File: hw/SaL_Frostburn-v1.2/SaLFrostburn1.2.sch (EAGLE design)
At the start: 99 parts, among them U1 ATSAMD21G-A, U3 ADXL345, U4 gps, Y1 32.768kHx, Y3 32MHz

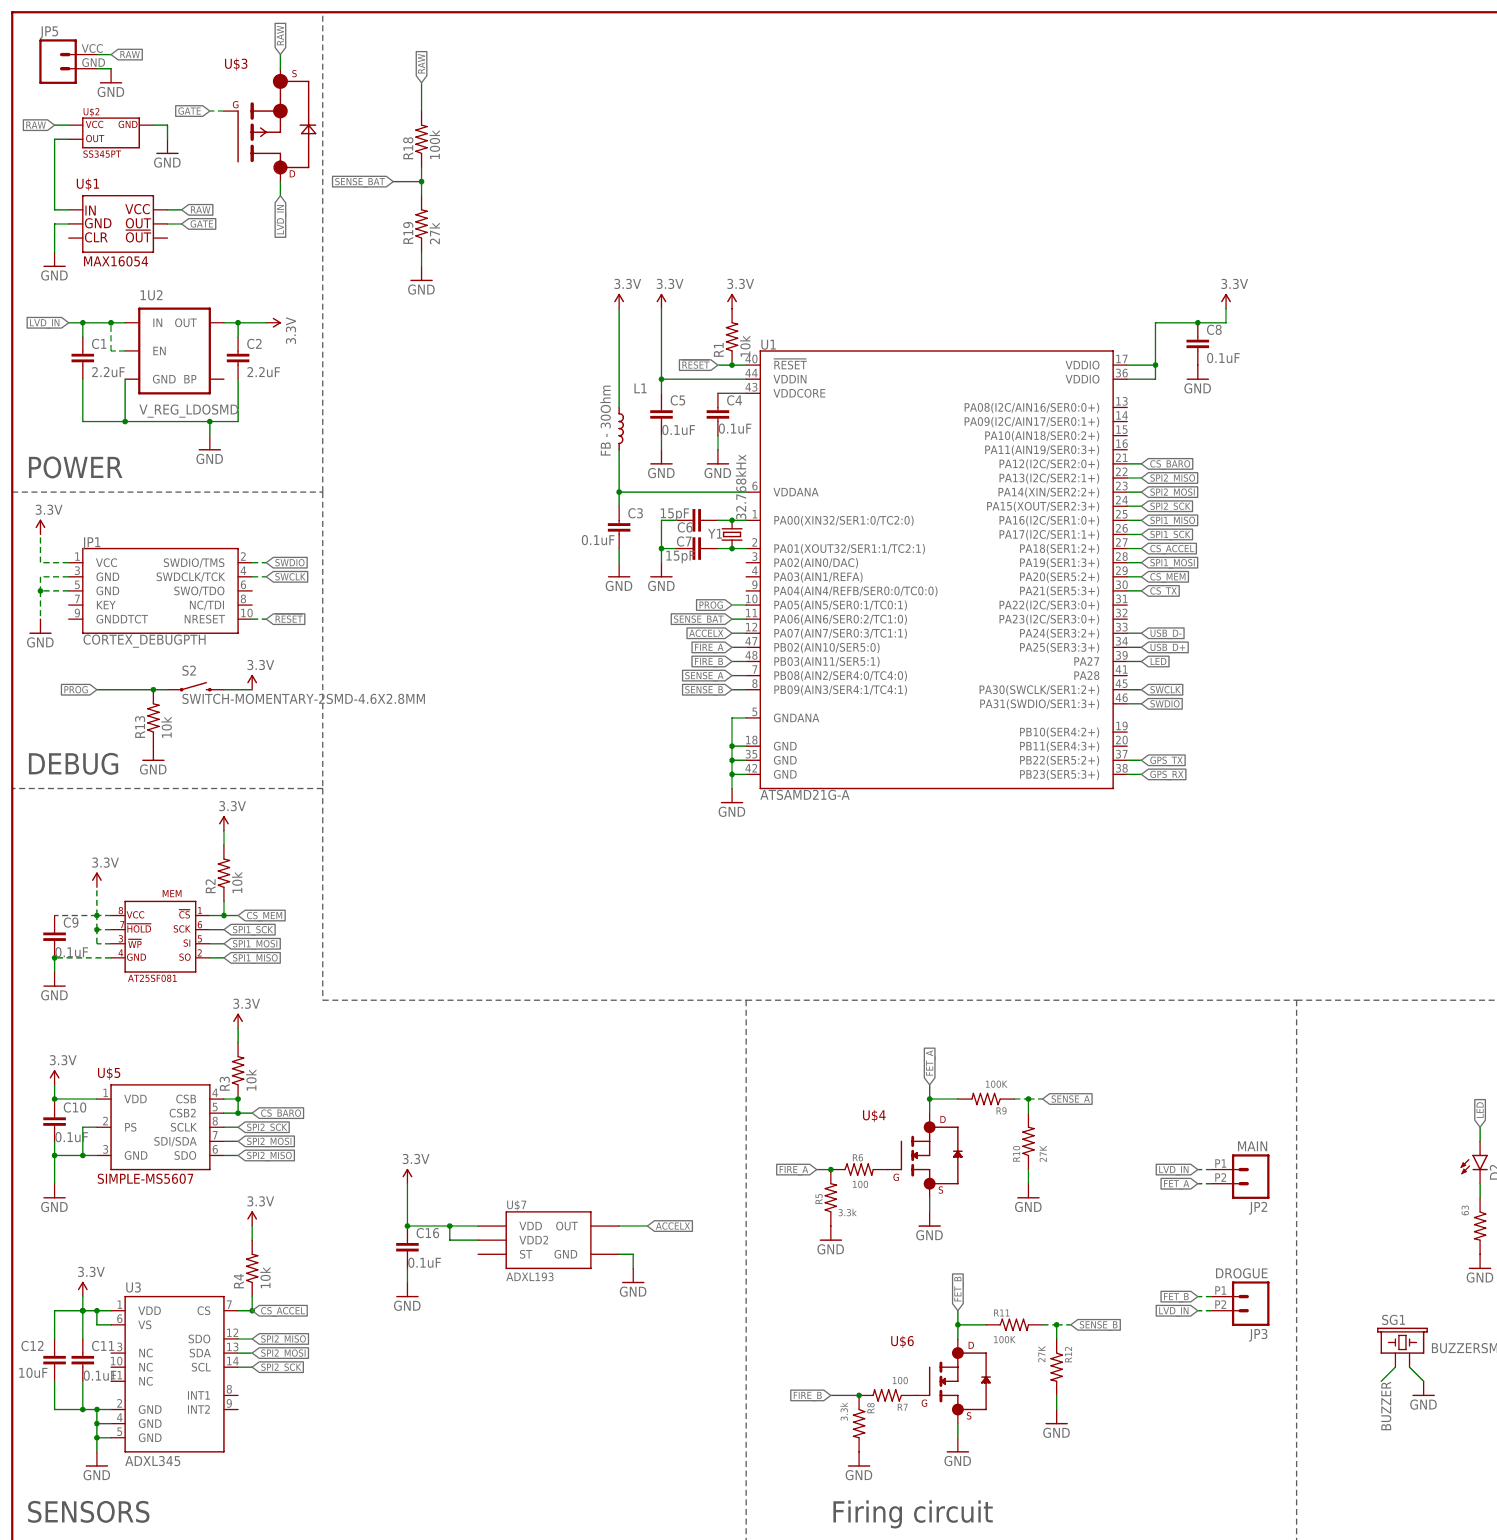
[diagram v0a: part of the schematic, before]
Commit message: added buzzer to 1.2 hw and setup 1.1 in studio
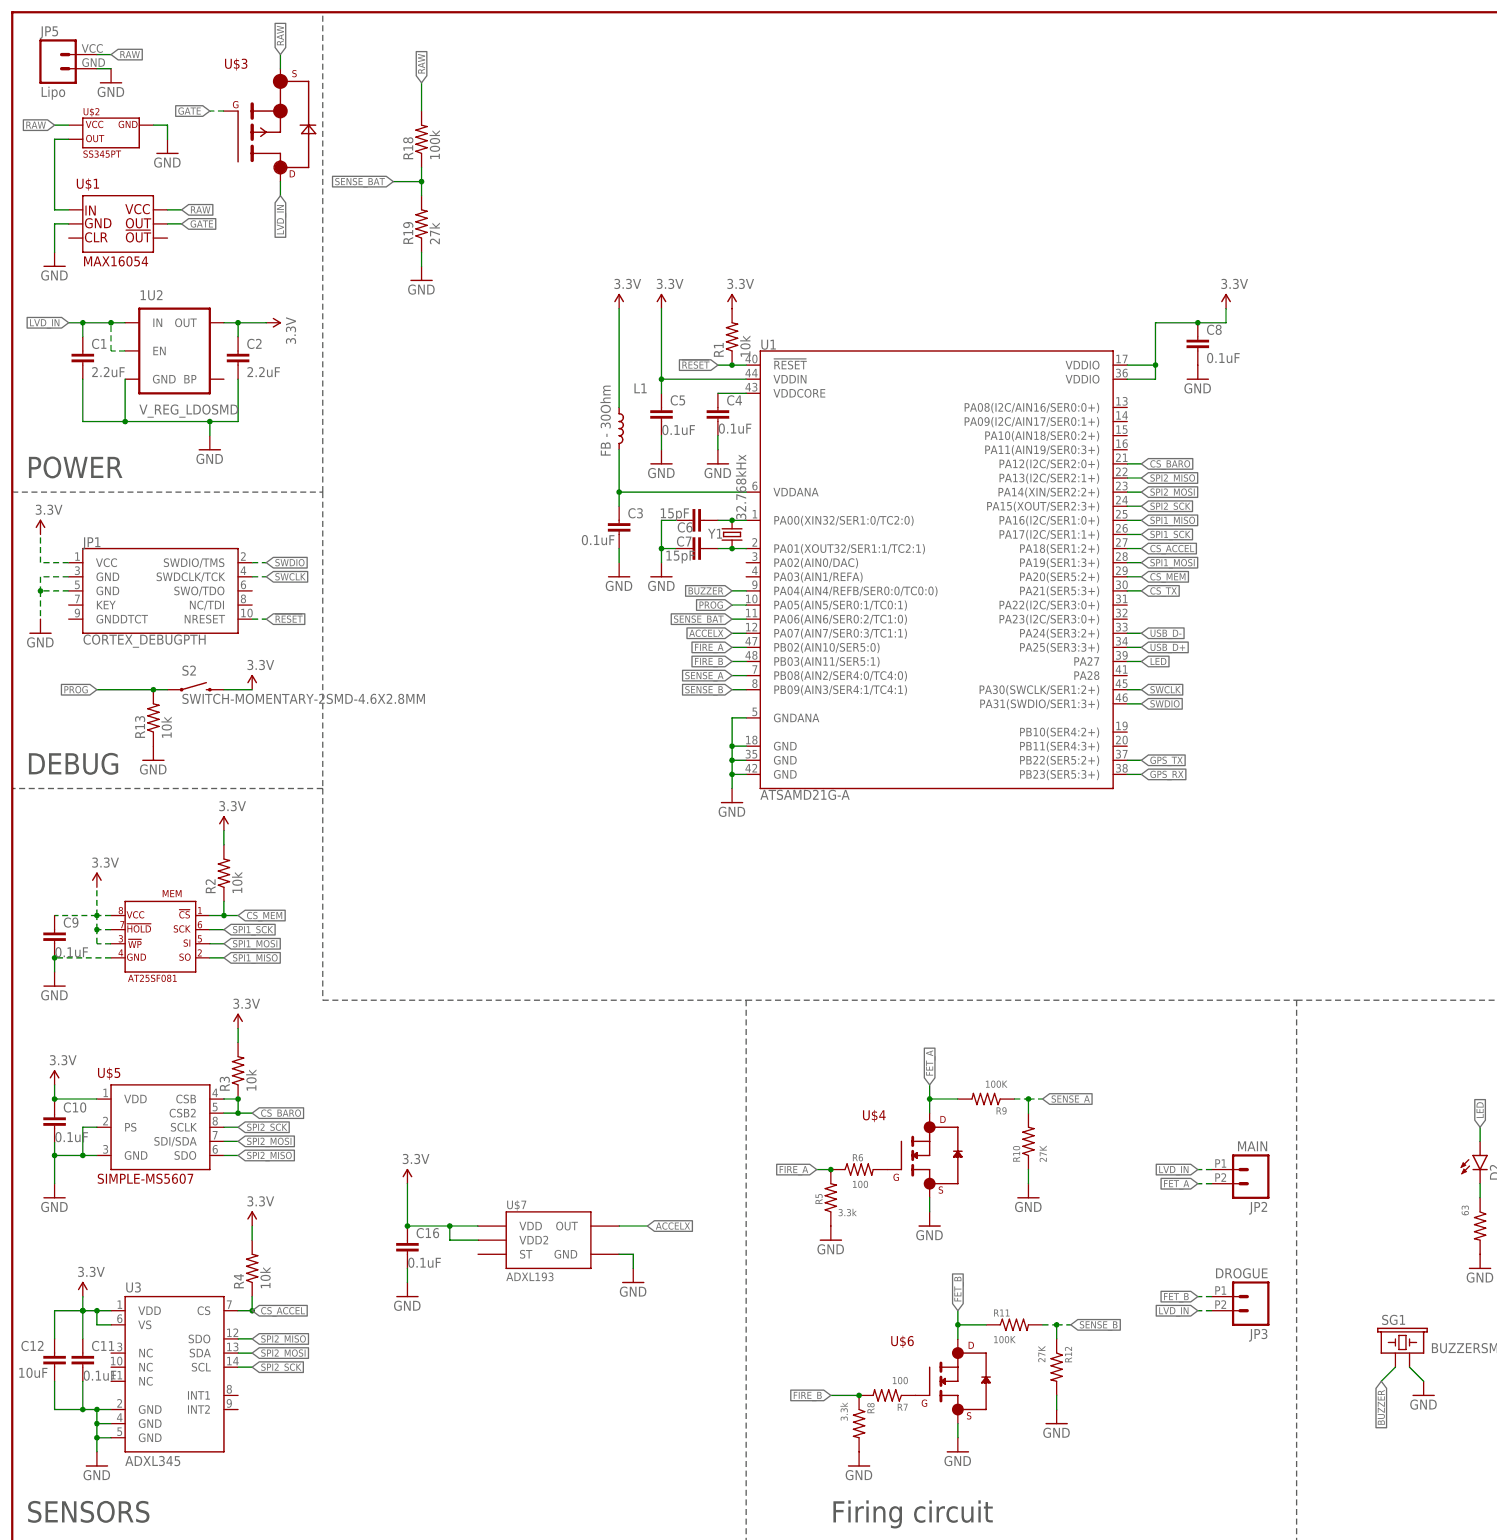
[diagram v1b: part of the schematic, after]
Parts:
- JP5: value (none) -> Lipo
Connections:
- net BUZZER: now also U1.PA04(AIN4/REFB/SER0:0/TC0:0)
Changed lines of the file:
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@@
 <part name="U$4" library="SaL-lib1" deviceset="SIS410DN" device=""/>
 <part name="U$6" library="SaL-lib1" deviceset="SIS410DN" device=""/>
-<part name="JP5" library="SparkFun-Connectors" deviceset="M02" device="4UCON-15767"/>
+<part name="JP5" library="SparkFun-Connectors" deviceset="M02" device="4UCON-15767" value="Lipo"/>
 <part name="STANDOFF4" library="SparkFun-Electromechanical" deviceset="STAND-OFF" device=""/>
 <part name="U$7" library="SparkFun-Sensors" deviceset="ADXL193" device=""/>
@@
 <pinref part="SG1" gate="G$1" pin="1"/>
 <wire x1="248.92" y1="35.56" x2="246.38" y2="33.02" width="0.1524" layer="91"/>
-<label x="246.38" y="33.02" size="1.778" layer="95" rot="R270"/>
-</segment>
-</net>
+<label x="246.38" y="33.02" size="1.27" layer="95" rot="R270" xref="yes"/>
+</segment>
+<segment>
+<pinref part="U1" gate="G$1" pin="PA04(AIN4/REFB/SER0:0/TC0:0)"/>
+<wire x1="132.08" y1="175.26" x2="129.54" y2="175.26" width="0.1524" layer="91"/>
+<label x="129.54" y="175.26" size="1.27" layer="95" rot="R180" xref="yes"/>
+</segment>
+</net>

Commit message: 1.2 hw sent to fab and some work on 1.1 code
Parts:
- removed FRAME1: FRAME-LEDGER, SparkFun-Aesthetics:FRAME-LEDGER
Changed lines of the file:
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@@
 <parts>
 <part name="U1" library="SparkFun-DigitalIC" deviceset="ATSAMD21G" device="-A"/>
-<part name="FRAME1" library="SparkFun-Aesthetics" deviceset="FRAME-LEDGER" device=""/>
 <part name="1U2" library="SparkFun-PowerIC" deviceset="V_REG_LDO" device="SMD"/>
 <part name="SUPPLY1" library="SparkFun-Aesthetics" deviceset="3.3V" device=""/>
@@
 <instances>
 <instance part="U1" gate="G$1" x="165.1" y="172.72"/>
-<instance part="FRAME1" gate="G$1" x="0" y="0"/>
-<instance part="FRAME1" gate="G$2" x="330.2" y="0"/>
 <instance part="1U2" gate="G$1" x="30.48" y="218.44"/>
 <instance part="SUPPLY1" gate="G$1" x="45.72" y="223.52" rot="R270"/>

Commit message: not real changes
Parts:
- added STANDOFF5: STAND-OFF, SparkFun-Electromechanical:STAND-OFF
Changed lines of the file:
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@@
 <?xml version="1.0" encoding="utf-8"?>
 <!DOCTYPE eagle SYSTEM "eagle.dtd">
-<eagle version="7.5.0">
+<eagle version="8.3.1">
 <drawing>
 <settings>
 <setting alwaysvectorfont="no"/>
+<setting keepoldvectorfont="yes"/>
 <setting verticaltext="up"/>
 </settings>
@@
 <part name="C16" library="SparkFun-Passives" deviceset="CAP" device="0402-CAP" value="0.1uF"/>
 <part name="SUPPLY24" library="SparkFun-Aesthetics" deviceset="3.3V" device=""/>
+<part name="STANDOFF5" library="SparkFun-Electromechanical" deviceset="STAND-OFF" device=""/>
 </parts>
 <sheets>
@@
 </instance>
 <instance part="SUPPLY24" gate="G$1" x="358.14" y="251.46"/>
+<instance part="STANDOFF5" gate="G$1" x="266.7" y="111.76"/>
 </instances>
 <busses>
